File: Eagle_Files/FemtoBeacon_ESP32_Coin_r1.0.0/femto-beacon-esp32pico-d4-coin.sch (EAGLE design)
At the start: 48 parts, among them IC1 ESP32-QFN_5X5

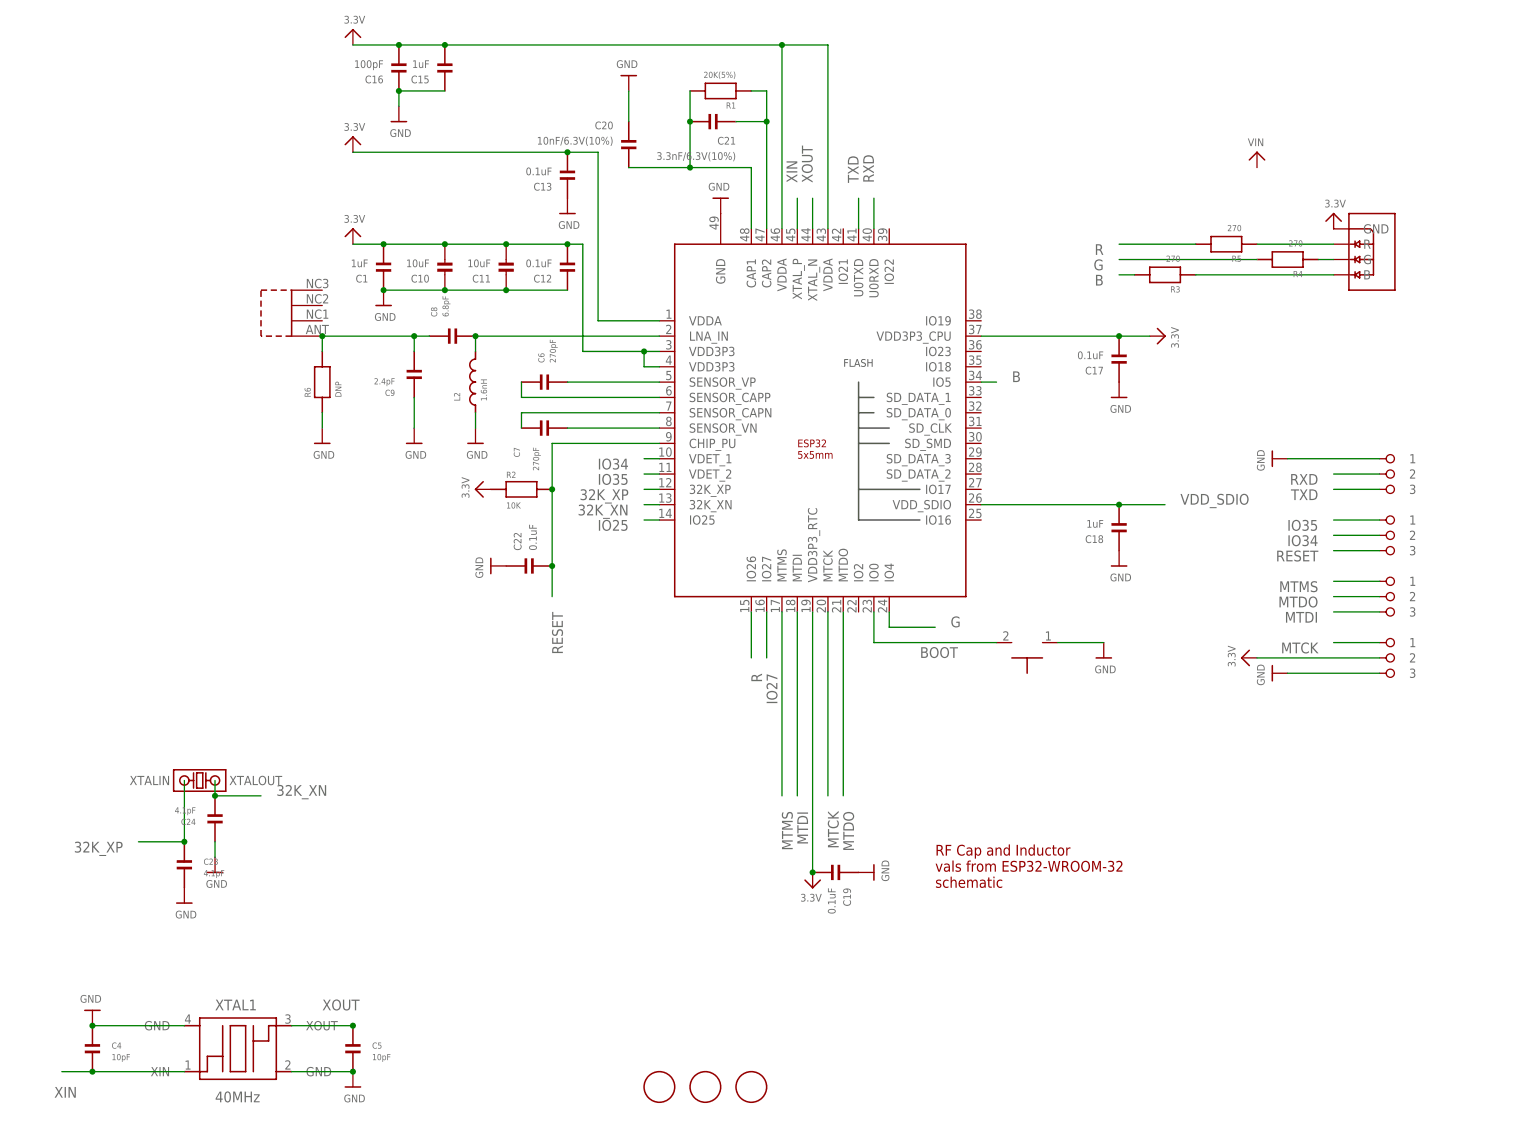
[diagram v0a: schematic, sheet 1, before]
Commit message: Adding new ESP32-PICO-D4 based coin with IMU and altimeter
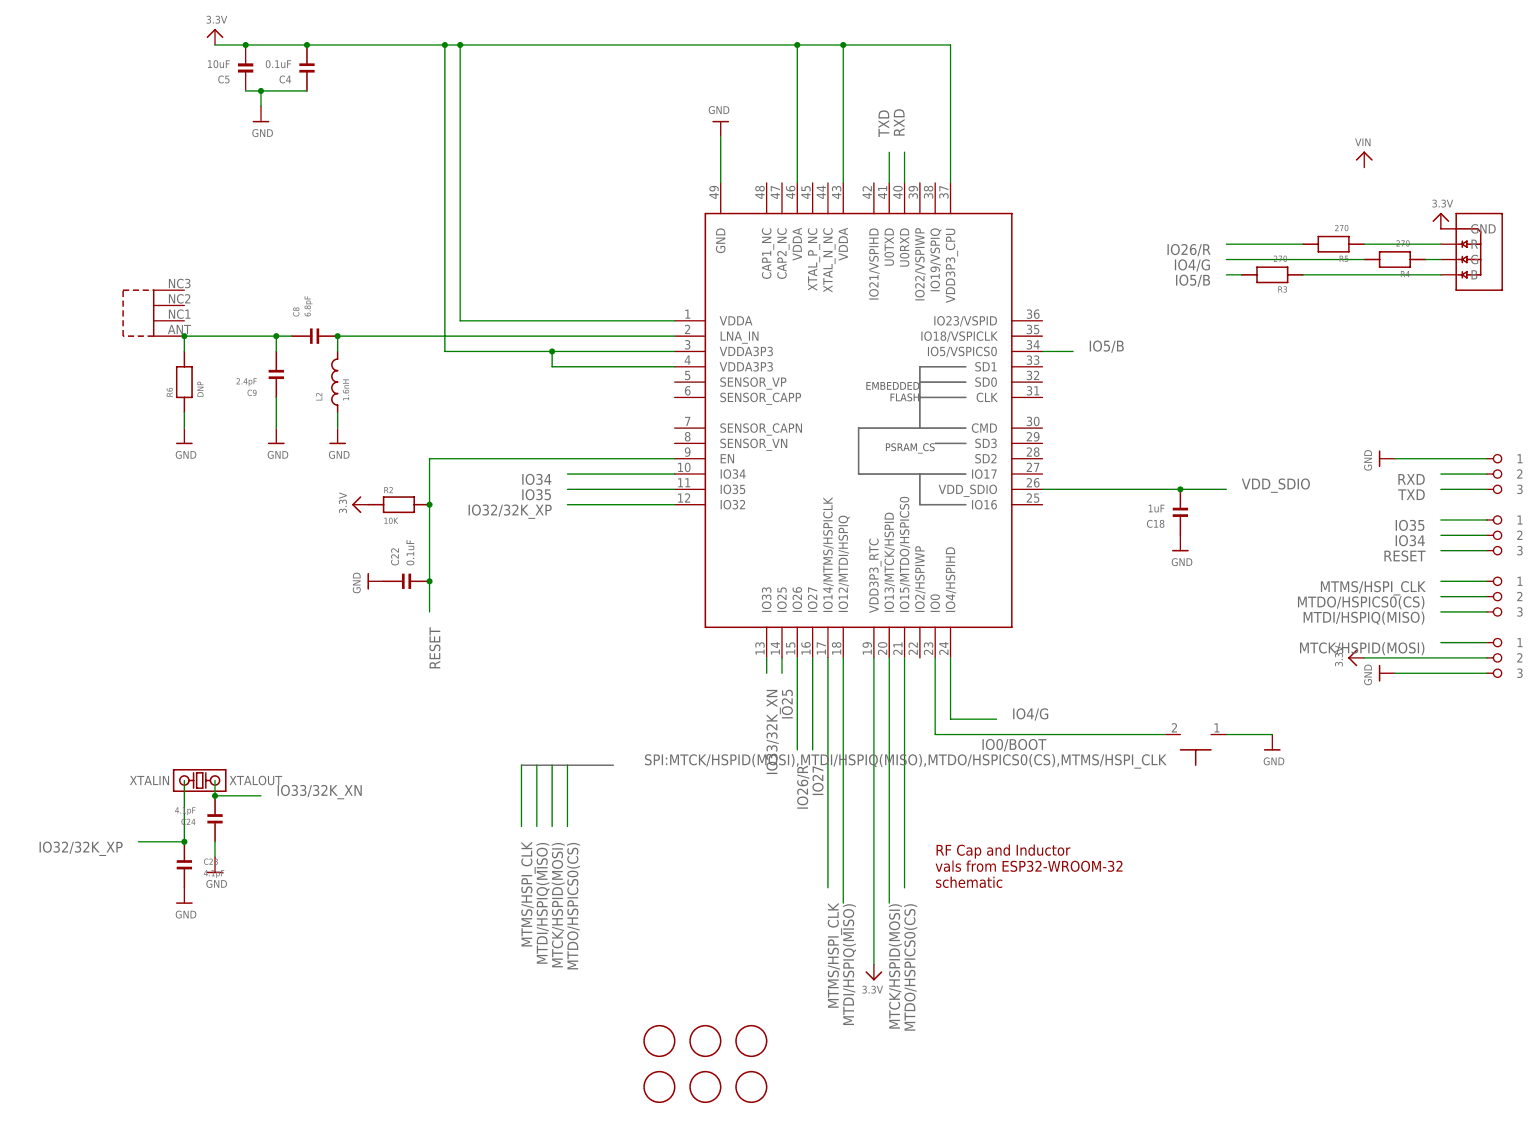
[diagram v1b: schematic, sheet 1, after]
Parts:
- removed C1, C15: 1uF, parts_0201:CAPACITOR_0201
- removed C10, C11: 10uF, microbuilder:CAP_CERAMIC_0603MP
- removed C12, C13, C17, C19: 0.1uF, parts_0201:CAPACITOR_0201
- removed C16: 100pF, parts_0201:CAPACITOR_0201
- removed C20: 10nF/6.3V(10%), parts_0201:CAPACITOR_0201
- removed C21: 3.3nF/6.3V(10%), parts_0201:CAPACITOR_0201
- removed C6, C7: 270pF, parts_0201:CAPACITOR_0201
- removed R1: 20K(5%), parts_0201:RESISTOR_0201
- removed XTAL1: 40MHz, crystals:FA-128
- added ALT1: MS5611-01BA03, freeimu:MS5611-01BA03
- added C25, C28, C29: 0.1uF, parts_0201:CAPACITOR_0201
- added FID4, FID5, FID6: FIDUCIAL, adafruit:FIDUCIAL
- added IMU1: ICM-20948, icm-20948:ICM-20948
- added SJ_FSYNC: DNP, microbuilder:SOLDERJUMPERCLOSED
- added U$1: 1X2_ROUND, pins_1.27mm_pitch:1X2_ROUND
- C4: value 10pF -> 0.1uF; MPN 02013A100JAT2A -> GRM033C80J104KE84D
- C5: value 10pF -> 10uF; device parts_0201:CAPACITOR_0201 -> microbuilder:CAP_CERAMIC_0603MP; MPN 02013A100JAT2A -> GRM188R61C106KAALD
- IC1: value ESP32-QFN_5X5 -> ESP32-PICO-D4; device esp32-wroom-32:ESP32-QFN_5X5 -> esp32-wroom-32:ESP32-PICO-D4; MPN ESP32-D2WD -> (none)
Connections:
- net BOOT renamed IO0/BOOT
- net R renamed IO26/R
- removed net 32K_XN: C24.P$1, IC1.32K_XN, XTAL2.XTALOUT
- removed net 32K_XP: C23.P$2, IC1.32K_XP, XTAL2.XTALIN
- removed net B: IC1.IO5, R3.2
- removed net G: IC1.IO4, R4.2
- removed net MTCK: IC1.MTCK, PIN_GPIO_A.1
- removed net MTDI: IC1.MTDI, PIN_GPIO_B.3
- removed net MTDO: IC1.MTDO, PIN_GPIO_B.2
- removed net MTMS: IC1.MTMS, PIN_GPIO_B.1
- removed net N$1: C6.P$1, IC1.SENSOR_VP
- removed net N$2: C6.P$2, IC1.SENSOR_CAPP
- removed net N$3: C7.P$2, IC1.SENSOR_VN
- removed net N$4: C7.P$1, IC1.SENSOR_CAPN
- removed net N$7: C21.P$2, IC1.CAP2, R1.1
- removed net N$9: C20.P$2, C21.P$1, IC1.CAP1, R1.2
- removed net XIN: C4.P$2, IC1.XTAL_P, XTAL1.XIN
- removed net XOUT: C5.P$2, IC1.XTAL_N, XTAL1.XOUT
- new net FSYNC_IMU: IMU1.FSYNC, SJ_FSYNC.1, U$1.2
- new net INT_WAKE_IMU: IMU1.INT, U$1.1
- new net IO32/32K_XP: C23.P$2, IC1.IO32, XTAL2.XTALIN
- new net IO33/32K_XN: C24.P$1, IC1.IO33, XTAL2.XTALOUT
- new net IO4/G: IC1.IO4/HSPIHD, R4.2
- new net IO5/B: IC1.IO5/VSPICS0, R3.2
- new net MTCK/HSPID(MOSI): ALT1.SDI/SDA, IC1.IO13/MTCK/HSPID, IMU1.SDA/SDI, PIN_GPIO_A.1
- new net MTDI/HSPIQ(MISO): ALT1.SDO, IC1.IO12/MTDI/HSPIQ, IMU1.SD0/AD0, PIN_GPIO_B.3
- new net MTDO/HSPICS0(CS): ALT1.CSB, IC1.IO15/MTDO/HSPICS0, IMU1.NCS, PIN_GPIO_B.2
- new net MTMS/HSPI_CLK: ALT1.SCLK, IC1.IO14/MTMS/HSPICLK, IMU1.SCL/SCLK, PIN_GPIO_B.1
- new net N$16: C29.P$2, IMU1.REGOUT
- net 3.3V: now also ALT1.VDD, C25.P$1, C28.P$2, C4.P$2, C5.P$2, IC1.VDDA3P3@1, IC1.VDDA3P3@2, IMU1.VDD, IMU1.VDDIO; no longer C1.P$2, C10.P$2, C11.P$2, C12.P$2, C13.P$2, C15.P$2, C16.P$2, C17.P$2, C19.P$2, IC1.VDD3P3@1, IC1.VDD3P3@2
- net GND: now also ALT1.GND, ALT1.PS, C25.P$2, C28.P$1, C29.P$1, IMU1.RESV@2, SJ_FSYNC.2; no longer C1.P$1, C10.P$1, C11.P$1, C12.P$1, C13.P$1, C15.P$1, C16.P$1, C17.P$1, C19.P$1, C20.P$1, XTAL1.GND@1, XTAL1.GND@2
- net IO34: now also IC1.IO34; no longer IC1.VDET_1
- net IO35: now also IC1.IO35; no longer IC1.VDET_2
- net RESET: now also IC1.EN; no longer IC1.CHIP_PU
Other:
- note added: "IMU + Altimeter"
- note added: "SENSOR MODULES"
- note removed: "USB"
- moved on the sheet: C18, C22, C4, C8, C9, L2, R2, R3, R4, R5, R6

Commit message: Current work on Hacker House board, and ESP32 coins
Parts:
- removed ALT1: MS5611-01BA03, freeimu:MS5611-01BA03
- removed C25, C28, C29: 0.1uF, parts_0201:CAPACITOR_0201
- removed IMU1: ICM-20948, icm-20948:ICM-20948
- removed SJ_FSYNC: DNP, microbuilder:SOLDERJUMPERCLOSED
- removed U$1: 1X2_ROUND, pins_1.27mm_pitch:1X2_ROUND
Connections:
- removed net FSYNC_IMU: IMU1.FSYNC, SJ_FSYNC.1, U$1.2
- removed net INT_WAKE_IMU: IMU1.INT, U$1.1
- removed net N$16: C29.P$2, IMU1.REGOUT
- new net IO18: IC1.IO18/VSPICLK
- new net IO23: IC1.IO23/VSPID
- net 3.3V: no longer ALT1.VDD, C25.P$1, C28.P$2, IMU1.VDD, IMU1.VDDIO
- net GND: no longer ALT1.GND, ALT1.PS, C25.P$2, C28.P$1, C29.P$1, IMU1.RESV@2, SJ_FSYNC.2
- net MTCK/HSPID(MOSI): no longer ALT1.SDI/SDA, IMU1.SDA/SDI
- net MTDI/HSPIQ(MISO): no longer ALT1.SDO, IMU1.SD0/AD0
- net MTDO/HSPICS0(CS): no longer ALT1.CSB, IMU1.NCS
- net MTMS/HSPI_CLK: no longer ALT1.SCLK, IMU1.SCL/SCLK
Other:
- note added: "IC, LPS"
- note removed: "IMU + Altimeter"
- note removed: "SENSOR MODULES"
